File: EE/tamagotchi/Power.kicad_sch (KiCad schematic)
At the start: 5 parts, among them J2 Conn_01x03_Pin, P1 USB_C_Plug_USB2.0, SW1 SW_SPST

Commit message: Generic Continutation Checkin
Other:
- note added: "TODO ESD"
- note added: "TODO TS?"
- moved on the sheet: JP1, SW1, U1
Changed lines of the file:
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@@
 	(generator_version "9.0")
 	(paper "A4")
+	(text "TODO ESD"
+		(exclude_from_sim no)
+		(at 59.944 92.71 0)
+		(effects
+			(font
+				(size 1.27 1.27)
+			)
+		)
+	)
 	(text "TODO pi filter / caps for VBUS"
 		(exclude_from_sim no)
@@
 	(text "Castelated board.\nSee: https://github.com/rolfluc/Batteryboard"
 		(exclude_from_sim no)
-		(at 152.654 87.122 0)
+		(at 150.114 96.012 0)
+		(effects
+			(font
+				(size 1.27 1.27)
+			)
+		)
+	)
+	(text "TODO TS?"
+		(exclude_from_sim no)
+		(at 145.034 70.612 0)
 		(effects
 			(font
@@
 	(wire
 		(pts
-			(xy 167.64 102.87) (xy 167.64 96.52)
+			(xy 165.1 111.76) (xy 165.1 105.41)
 		)
 		(stroke
@@
 	(wire
 		(pts
-			(xy 134.62 102.87) (xy 138.43 102.87)
+			(xy 132.08 111.76) (xy 135.89 111.76)
 		)
 		(stroke
@@
 	(wire
 		(pts
-			(xy 167.64 96.52) (xy 176.53 96.52)
+			(xy 165.1 105.41) (xy 173.99 105.41)
 		)
 		(stroke
@@
 	(wire
 		(pts
-			(xy 134.62 97.79) (xy 134.62 102.87)
+			(xy 132.08 106.68) (xy 132.08 111.76)
 		)
 		(stroke
@@
 	(wire
 		(pts
-			(xy 165.1 107.95) (xy 177.8 107.95)
+			(xy 162.56 116.84) (xy 175.26 116.84)
 		)
 		(stroke
@@
 	(wire
 		(pts
-			(xy 165.1 102.87) (xy 167.64 102.87)
+			(xy 162.56 111.76) (xy 165.1 111.76)
 		)
 		(stroke
@@
 	)
 	(label "INT_N"
-		(at 138.43 110.49 180)
+		(at 135.89 119.38 180)
 		(effects
 			(font
@@
 	)
 	(label "SDA"
-		(at 138.43 107.95 180)
+		(at 135.89 116.84 180)
 		(effects
 			(font
@@
 	)
 	(label "SCL"
-		(at 138.43 105.41 180)
+		(at 135.89 114.3 180)
 		(effects
 			(font
@@
 	)
 	(label "SWITCH"
-		(at 165.1 110.49 0)
+		(at 162.56 119.38 0)
 		(effects
 			(font
@@
 	)
 	(label "VSYS"
-		(at 165.1 105.41 0)
+		(at 162.56 114.3 0)
 		(effects
 			(font
@@
 	)
 	(label "VBAT"
-		(at 185.42 107.95 270)
+		(at 182.88 116.84 270)
 		(effects
 			(font
@@
 	)
 	(label "TS"
-		(at 165.1 113.03 0)
+		(at 162.56 121.92 0)
 		(effects
 			(font
@@
 	)
 	(label "CE_N"
-		(at 138.43 113.03 180)
+		(at 135.89 121.92 180)
 		(effects
 			(font
@@
 	)
 	(label "SWITCH"
-		(at 182.88 123.19 90)
+		(at 180.34 132.08 90)
 		(effects
 			(font
@@
 	(symbol
 		(lib_id "power:VBUS")
-		(at 134.62 97.79 0)
+		(at 132.08 106.68 0)
 		(unit 1)
 		(exclude_from_sim no)
@@
 		(fields_autoplaced yes)
 		(property "Reference" "#PWR06"
-			(at 134.62 101.6 0)
+			(at 132.08 110.49 0)
 			(effects
 				(font
@@
 		)
 		(property "Value" "VBUS"
-			(at 134.62 93.6569 0)
+			(at 132.08 102.5469 0)
 			(effects
 				(font
@@
 		)
 		(property "Footprint" ""
-			(at 134.62 97.79 0)
+			(at 132.08 106.68 0)
 			(effects
 				(font
@@
 		)
 		(property "Datasheet" ""
-			(at 134.62 97.79 0)
+			(at 132.08 106.68 0)
 			(effects
 				(font
@@
 		)
 		(property "Description" "Power symbol creates a global label with name \"VBUS\""
-			(at 134.62 97.79 0)
+			(at 132.08 106.68 0)
 			(effects
 				(font
@@
 	(symbol
 		(lib_id "power:GND")
-		(at 176.53 96.52 0)
+		(at 173.99 105.41 0)
 		(unit 1)
 		(exclude_from_sim no)
@@
 		(fields_autoplaced yes)
 		(property "Reference" "#PWR04"
-			(at 176.53 102.87 0)
+			(at 173.99 111.76 0)
 			(effects
 				(font
@@
 		)
 		(property "Value" "GND"
-			(at 176.53 100.6531 0)
+			(at 173.99 109.5431 0)
 			(effects
 				(font
@@
 		)
 		(property "Footprint" ""
-			(at 176.53 96.52 0)
+			(at 173.99 105.41 0)
 			(effects
 				(font
@@
 		)
 		(property "Datasheet" ""
-			(at 176.53 96.52 0)
+			(at 173.99 105.41 0)
 			(effects
 				(font
@@
 		)
 		(property "Description" "Power symbol creates a global label with name \"GND\" , ground"
-			(at 176.53 96.52 0)
+			(at 173.99 105.41 0)
 			(effects
 				(font
@@
 	(symbol
 		(lib_id "New_Library:bq_castelated")
-		(at 161.29 118.11 0)
+		(at 158.75 127 0)
 		(unit 1)
 		(exclude_from_sim no)
@@
 		(fields_autoplaced yes)
 		(property "Reference" "U1"
-			(at 151.765 96.3125 0)
+			(at 149.225 105.2025 0)
 			(effects
 				(font
@@
 		)
 		(property "Value" "~"
-			(at 151.765 98.7368 0)
+			(at 149.225 107.6268 0)
 			(effects
 				(font
@@
 		)
 		(property "Footprint" ""
-			(at 161.29 118.11 0)
+			(at 158.75 127 0)
 			(effects
 				(font
@@
 		)
 		(property "Datasheet" ""
-			(at 161.29 118.11 0)
+			(at 158.75 127 0)
 			(effects
 				(font
@@
 		)
 		(property "Description" ""
-			(at 161.29 118.11 0)
+			(at 158.75 127 0)
 			(effects
 				(font
@@
 	(symbol
 		(lib_id "Switch:SW_SPST")
-		(at 182.88 128.27 90)
+		(at 180.34 137.16 90)
 		(unit 1)
 		(exclude_from_sim no)
@@
 		(fields_autoplaced yes)
 		(property "Reference" "SW1"
-			(at 184.023 127.0578 90)
+			(at 181.483 135.9478 90)
 			(effects
 				(font
@@
 		)
 		(property "Value" "SW_SPST"
-			(at 184.023 129.4821 90)
+			(at 181.483 138.3721 90)
 			(effects
 				(font
@@
 		)
 		(property "Footprint" ""
-			(at 182.88 128.27 0)
+			(at 180.34 137.16 0)
 			(effects
 				(font
@@
 		)
 		(property "Datasheet" "~"
-			(at 182.88 128.27 0)
+			(at 180.34 137.16 0)
 			(effects
 				(font
@@
 		)
 		(property "Description" "Single Pole Single Throw (SPST) switch"
-			(at 182.88 128.27 0)
+			(at 180.34 137.16 0)
 			(effects
 				(font
@@
 	(symbol
 		(lib_id "Jumper:SolderJumper_2_Bridged")
-		(at 181.61 107.95 180)
+		(at 179.07 116.84 180)
 		(unit 1)
 		(exclude_from_sim no)
@@
 		(fields_autoplaced yes)
 		(property "Reference" "JP1"
-			(at 181.61 102.9165 0)
+			(at 179.07 111.8065 0)
 			(effects
 				(font
@@
 		)
 		(property "Value" "SolderJumper_2_Bridged"
-			(at 181.61 105.3408 0)
+			(at 179.07 114.2308 0)
 			(effects
 				(font
@@
 		)
 		(property "Footprint" ""
-			(at 181.61 107.95 0)
+			(at 179.07 116.84 0)
 			(effects
 				(font
@@
 		)
 		(property "Datasheet" "~"
-			(at 181.61 107.95 0)
+			(at 179.07 116.84 0)
 			(effects
 				(font
@@
 		)
 		(property "Description" "Solder Jumper, 2-pole, closed/bridged"
-			(at 181.61 107.95 0)
+			(at 179.07 116.84 0)
 			(effects
 				(font
@@
 	(symbol
 		(lib_id "power:GND")
-		(at 182.88 133.35 0)
+		(at 180.34 142.24 0)
 		(unit 1)
 		(exclude_from_sim no)
@@
 		(fields_autoplaced yes)
 		(property "Reference" "#PWR05"
-			(at 182.88 139.7 0)
+			(at 180.34 148.59 0)
 			(effects
 				(font
@@
 		)
 		(property "Value" "GND"
-			(at 182.88 137.4831 0)
+			(at 180.34 146.3731 0)
 			(effects
 				(font
@@
 		)
 		(property "Footprint" ""
-			(at 182.88 133.35 0)
+			(at 180.34 142.24 0)
 			(effects
 				(font
@@
 		)
 		(property "Datasheet" ""
-			(at 182.88 133.35 0)
+			(at 180.34 142.24 0)
 			(effects
 				(font
@@
 		)
 		(property "Description" "Power symbol creates a global label with name \"GND\" , ground"
-			(at 182.88 133.35 0)
-			(effects
-				(font
+			(at 180.34 142.24 0)
+			(effects
+				(font

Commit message: Minor Update pre Display add
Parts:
- added D13: D_Zener, symbol Device:D_Zener
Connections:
- net GND: now also D13.2 (A)
- net VBUS: now also D13.1 (K); no longer U1.1 (VBUS)
- new net VBUS_FILT: U1.1 (VBUS)
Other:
- note removed: "TODO ESD"
- note removed: "TODO pi filter / caps for VBUS"
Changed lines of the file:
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@@
 	(generator_version "9.0")
 	(paper "A4")
-	(text "TODO ESD"
-		(exclude_from_sim no)
-		(at 59.944 92.71 0)
-		(effects
-			(font
-				(size 1.27 1.27)
-			)
-		)
-	)
-	(text "TODO pi filter / caps for VBUS"
-		(exclude_from_sim no)
-		(at 61.722 95.25 0)
-		(effects
-			(font
-				(size 1.27 1.27)
-			)
-		)
-	)
 	(text "Castelated board.\nSee: https://github.com/rolfluc/Batteryboard"
 		(exclude_from_sim no)
@@
 	(wire
 		(pts
-			(xy 132.08 106.68) (xy 132.08 111.76)
+			(xy 46.99 105.41) (xy 46.99 102.87)
 		)
 		(stroke
@@
 	(wire
 		(pts
-			(xy 46.99 105.41) (xy 46.99 102.87)
+			(xy 162.56 116.84) (xy 175.26 116.84)
 		)
 		(stroke
@@
 	(wire
 		(pts
-			(xy 162.56 116.84) (xy 175.26 116.84)
+			(xy 162.56 111.76) (xy 165.1 111.76)
 		)
 		(stroke
@@
 		)
 	)
-	(wire
-		(pts
-			(xy 162.56 111.76) (xy 165.1 111.76)
-		)
-		(stroke
-			(width 0)
-			(type default)
-		)
-	)
 	(label "INT_N"
 		(at 135.89 119.38 180)
@@
 	(label "SWITCH"
 		(at 180.34 132.08 90)
+		(effects
+			(font
+				(size 1.27 1.27)
+			)
+			(justify left bottom)
+		)
+	)
+	(label "VBUS_FILT"
+		(at 132.08 111.76 90)
 		(effects
 			(font
@@
 	)
 	(symbol
-		(lib_id "power:VBUS")
-		(at 132.08 106.68 0)
-		(unit 1)
-		(exclude_from_sim no)
-		(in_bom yes)
-		(on_board yes)
-		(dnp no)
-		(fields_autoplaced yes)
-		(property "Reference" "#PWR06"
-			(at 132.08 110.49 0)
-			(effects
-				(font
-					(size 1.27 1.27)
-				)
-				(hide yes)
-			)
-		)
-		(property "Value" "VBUS"
-			(at 132.08 102.5469 0)
-			(effects
-				(font
-					(size 1.27 1.27)
-				)
-			)
-		)
-		(property "Footprint" ""
-			(at 132.08 106.68 0)
-			(effects
-				(font
-					(size 1.27 1.27)
-				)
-				(hide yes)
-			)
-		)
-		(property "Datasheet" ""
-			(at 132.08 106.68 0)
-			(effects
-				(font
-					(size 1.27 1.27)
-				)
-				(hide yes)
-			)
-		)
-		(property "Description" "Power symbol creates a global label with name \"VBUS\""
-			(at 132.08 106.68 0)
-			(effects
-				(font
-					(size 1.27 1.27)
-				)
-				(hide yes)
-			)
-		)
-		(pin "1"
-		)
-		(instances
-			(project "tamagotchi"
-				(path "/47ffaef6-4682-4a87-a393-bad1a10963be/0f9f9e1b-dcd6-4194-955e-d48be8be13d1"
-					(reference "#PWR06")
-					(unit 1)
-				)
-			)
-		)
-	)
-	(symbol
 		(lib_id "power:GND")
 		(at 173.99 105.41 0)
@@
 	)
 	(symbol
+		(lib_id "Device:D_Zener")
+		(at 73.66 107.95 270)
+		(unit 1)
+		(exclude_from_sim no)
+		(in_bom yes)
+		(on_board yes)
+		(dnp no)
+		(fields_autoplaced yes)
+		(property "Reference" "D13"
+			(at 76.2 106.6799 90)
+			(effects
+				(font
+					(size 1.27 1.27)
+				)
+				(justify left)
+			)
+		)
+		(property "Value" "D_Zener"
+			(at 76.2 109.2199 90)
+			(effects
+				(font
+					(size 1.27 1.27)
+				)
+				(justify left)
+			)
+		)
+		(property "Footprint" ""
+			(at 73.66 107.95 0)
+			(effects
+				(font
+					(size 1.27 1.27)
+				)
+				(hide yes)
+			)
+		)
+		(property "Datasheet" "~"
+			(at 73.66 107.95 0)
+			(effects
+				(font
+					(size 1.27 1.27)
+				)
+				(hide yes)
+			)
+		)
+		(property "Description" "Zener diode"
+			(at 73.66 107.95 0)
+			(effects
+				(font
+					(size 1.27 1.27)
+				)
+				(hide yes)
+			)
+		)
+		(pin "1"
+		)
+		(pin "2"
+		)
+		(instances
+			(project ""
+				(path "/47ffaef6-4682-4a87-a393-bad1a10963be/0f9f9e1b-dcd6-4194-955e-d48be8be13d1"
+					(reference "D13")
+					(unit 1)
+				)
+			)
+		)
+	)
+	(symbol
 		(lib_id "power:VBUS")
 		(at 46.99 102.87 0)
@@
 					(unit 1)
 				)
+			)
+		)
+	)
+	(symbol
+		(lib_id "power:VBUS")
+		(at 73.66 104.14 0)
+		(unit 1)
+		(exclude_from_sim no)
+		(in_bom yes)
+		(on_board yes)
+		(dnp no)
+		(fields_autoplaced yes)
+		(property "Reference" "#PWR029"
+			(at 73.66 107.95 0)
+			(effects
+				(font
+					(size 1.27 1.27)
+				)
+				(hide yes)
+			)
+		)
+		(property "Value" "VBUS"
+			(at 73.66 100.0069 0)
+			(effects
+				(font
+					(size 1.27 1.27)
+				)
+			)
+		)
+		(property "Footprint" ""
+			(at 73.66 104.14 0)
+			(effects
+				(font
+					(size 1.27 1.27)
+				)
+				(hide yes)
+			)
+		)
+		(property "Datasheet" ""
+			(at 73.66 104.14 0)
+			(effects
+				(font
+					(size 1.27 1.27)
+				)
+				(hide yes)
+			)
+		)
+		(property "Description" "Power symbol creates a global label with name \"VBUS\""
+			(at 73.66 104.14 0)
+			(effects
+				(font
+					(size 1.27 1.27)
+				)
+				(hide yes)
+			)
+		)
+		(pin "1"
+		)
+		(instances
+			(project "tamagotchi"
+				(path "/47ffaef6-4682-4a87-a393-bad1a10963be/0f9f9e1b-dcd6-4194-955e-d48be8be13d1"
+					(reference "#PWR029")
+					(unit 1)
+				)
+			)
+		)
+	)
+	(symbol
+		(lib_id "power:GND")
+		(at 73.66 111.76 0)
+		(unit 1)
+		(exclude_from_sim no)
+		(in_bom yes)
+		(on_board yes)
+		(dnp no)
+		(fields_autoplaced yes)
+		(property "Reference" "#PWR030"
+			(at 73.66 118.11 0)
+			(effects
+				(font
+					(size 1.27 1.27)
+				)
+				(hide yes)
+			)
+		)
+		(property "Value" "GND"
+			(at 73.66 115.8931 0)
+			(effects
+				(font
+					(size 1.27 1.27)
+				)
+			)
+		)
+		(property "Footprint" ""
+			(at 73.66 111.76 0)
+			(effects
+				(font
+					(size 1.27 1.27)
+				)
+				(hide yes)
+			)
+		)
+		(property "Datasheet" ""
+			(at 73.66 111.76 0)
+			(effects
+				(font
+					(size 1.27 1.27)
+				)
+				(hide yes)
+			)
+		)
+		(property "Description" "Power symbol creates a global label with name \"GND\" , ground"
+			(at 73.66 111.76 0)
+			(effects
+				(font
+					(size 1.27 1.27)
+				)
+				(hide yes)
+			)
+		)
+		(pin "1"
+		)
+		(instances
+			(project "tamagotchi"
+				(path "/47ffaef6-4682-4a87-a393-bad1a10963be/0f9f9e1b-dcd6-4194-955e-d48be8be13d1"
+					(reference "#PWR030")
+					(unit 1)
+				)

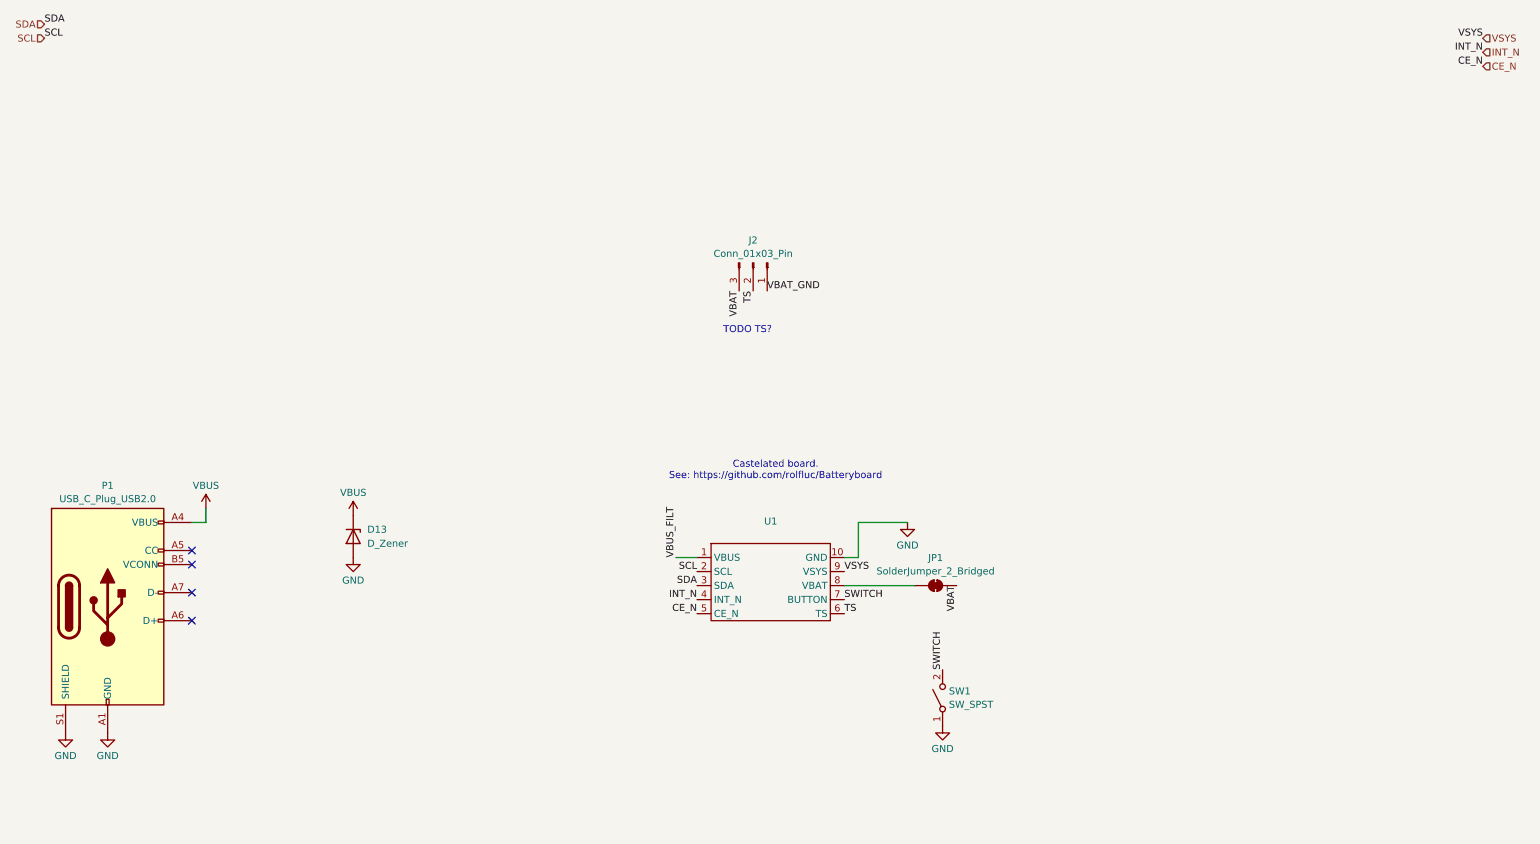
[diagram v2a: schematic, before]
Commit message: WIP - added 3D / footprints for devices. RGY LEDs aren't right
Need to do more outling / ect. super rough placement for everything.
LED footprint for RGY appears just wrong
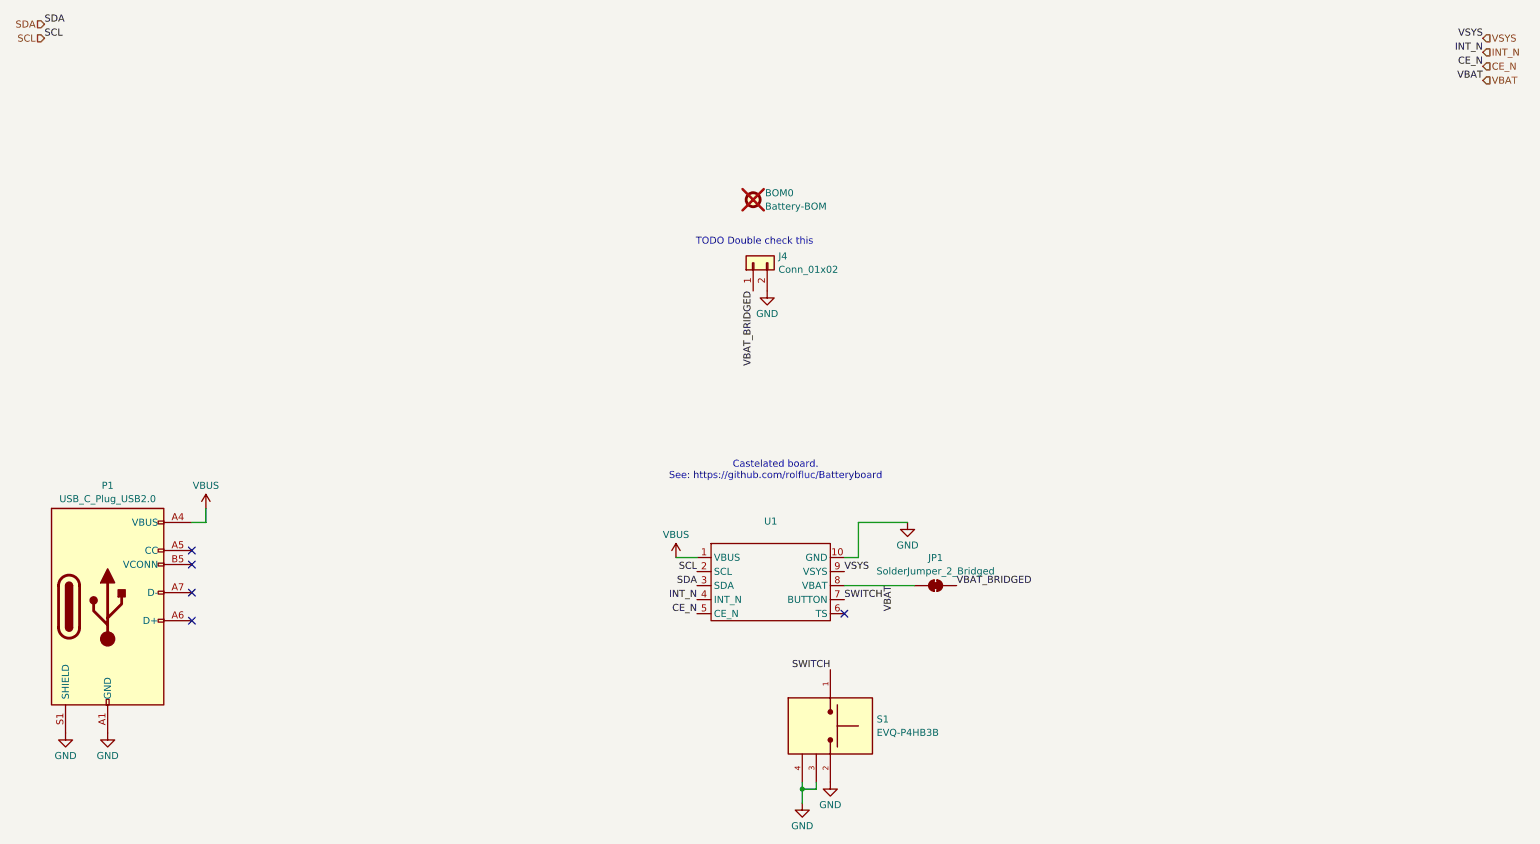
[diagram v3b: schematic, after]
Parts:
- removed D13: D_Zener, symbol Device:D_Zener
- removed J2: Conn_01x03_Pin, symbol Connector:Conn_01x03_Pin
- removed SW1: SW_SPST, symbol Switch:SW_SPST
- added BOM0: Battery-BOM, symbol Mechanical:Fiducial
- added J4: Conn_01x02, symbol Connector_Generic:Conn_01x02
- added S1: EVQ-P4HB3B, Library:SW_EVQ-P4HB3B, symbol New_Library:EVQ-P4HB3B
- JP1: footprint (none) -> Jumper:SolderJumper-2_P1.3mm_Bridged2Bar_RoundedPad1.0x1.5mm
- P1: footprint (none) -> Connector_USB:USB_C_Receptacle_GCT_USB4085
- U1: footprint (none) -> Library:BatteryBoard
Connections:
- net VBUS_FILT is gone; now on net VBUS: U1.1 (VBUS)
- net GND: now also J4.2 (Pin_2), S1.2, S1.3, S1.4
- net SWITCH: now also S1.1
- net VBAT: now also JP1.2 (B), U1.8 (VBAT); no longer JP1.1 (A)
- net TS: no longer names the net of U1.6 (TS)
- new net VBAT_BRIDGED: J4.1 (Pin_1), JP1.1 (A)
- no-connect marks 4 -> 5
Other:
- note added: "TODO Double check this"
- note removed: "TODO TS?"
